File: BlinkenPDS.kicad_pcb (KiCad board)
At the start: 4 copper layers, 129 x 99 mm, 257 parts, among them CN1 PDS_LB_MALE, CN2 PDS_PT_FEMALE RA, CN3 PDS_PT_FEMALE ST, U1 74HC14D, U10 74HC14D, U11 74HC14D, U12 74HC14D, U13 74HC14D, U14 74HC14D, U15 74HC14D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

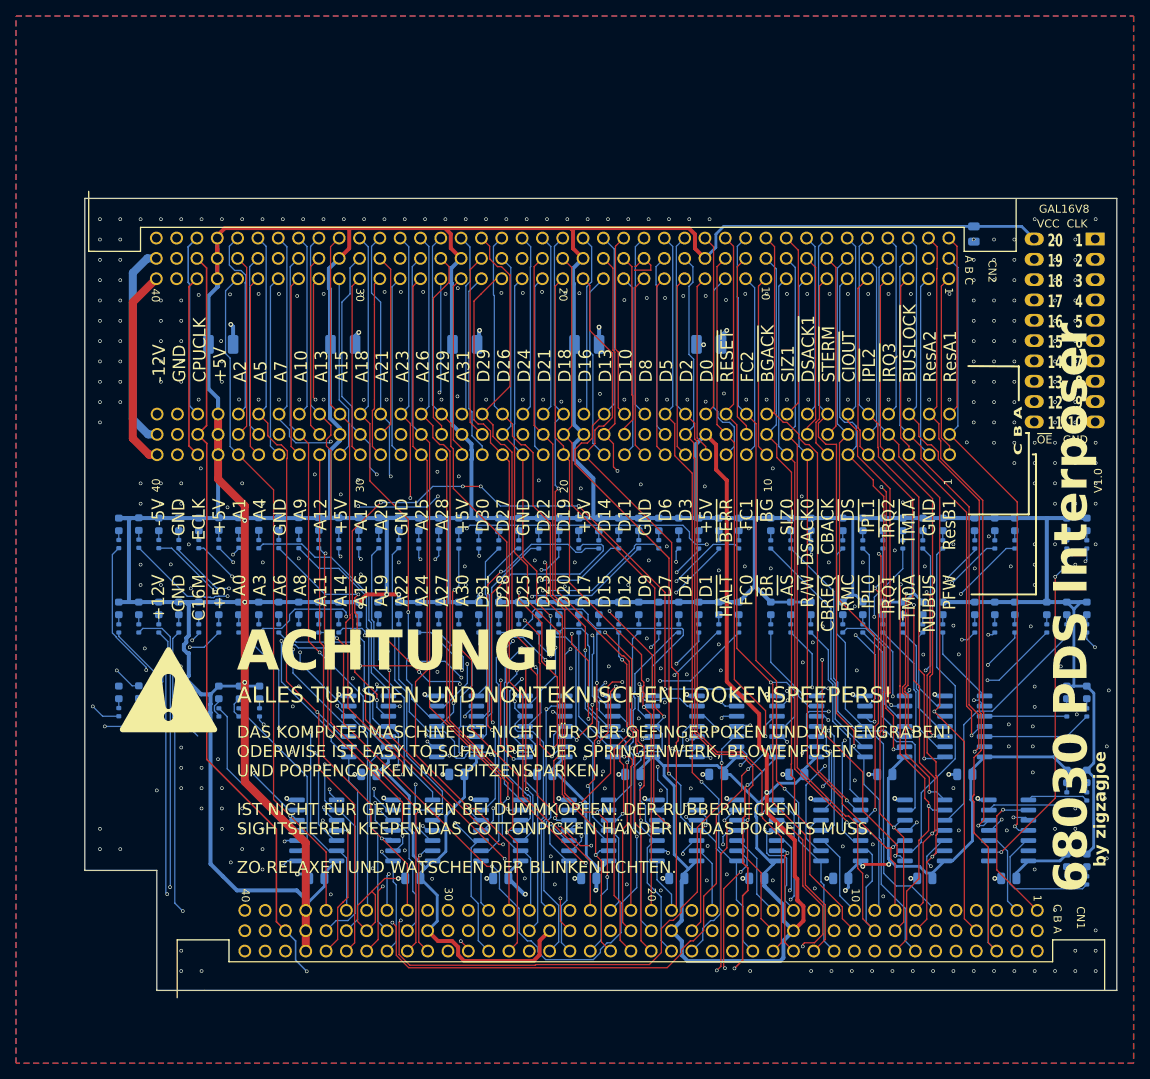
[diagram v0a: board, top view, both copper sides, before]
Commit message: remove PFW, add CACHE, updated production files
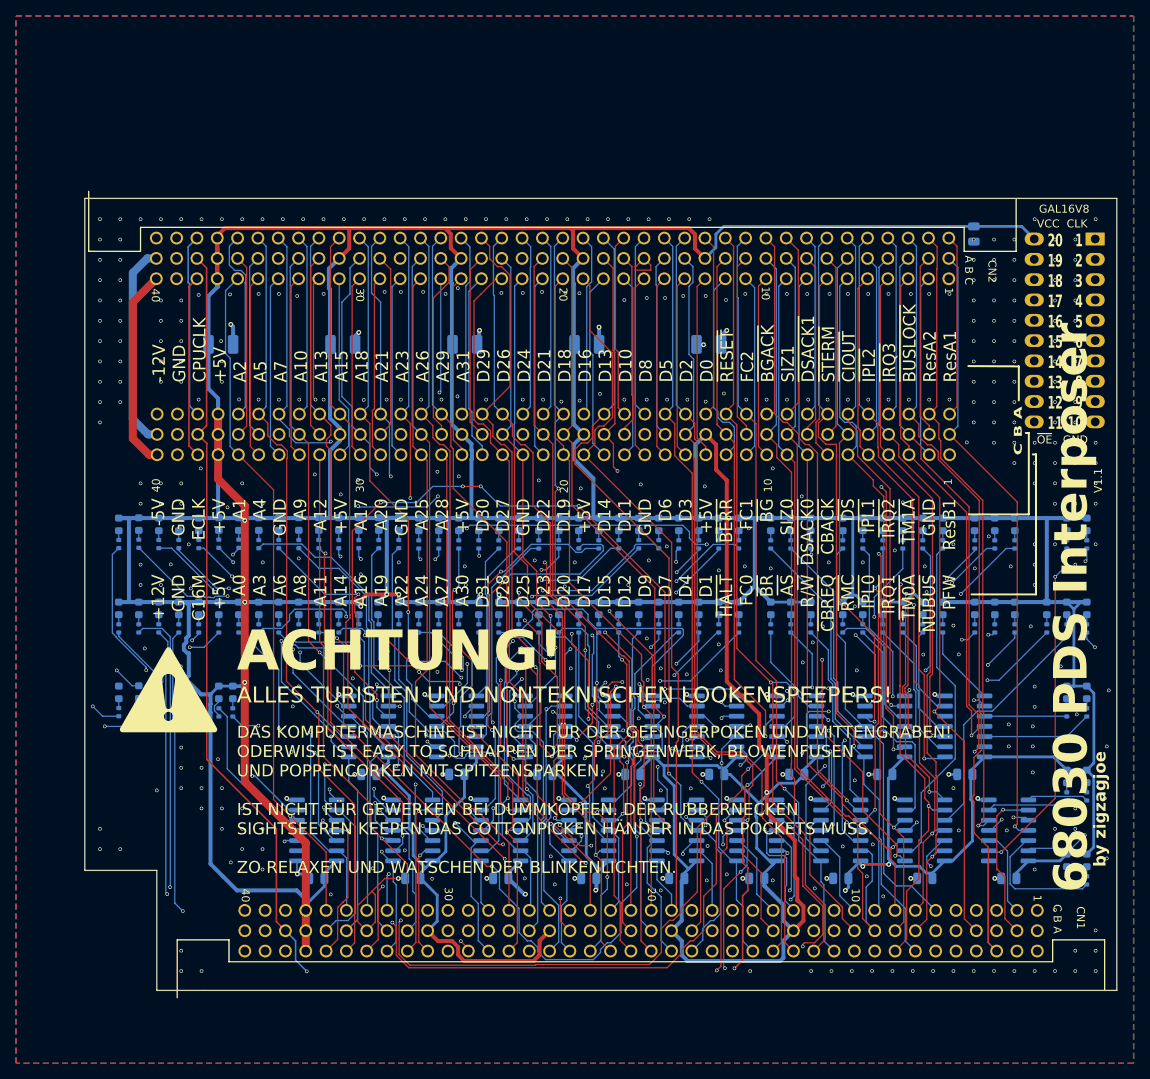
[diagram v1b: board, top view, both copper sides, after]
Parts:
- removed D67: C, SockeBooster:LED_0603_1608Metric_Label
- removed R68: 510, SockeBooster:R_0402_1005Metric_NoLabel
- moved D66 3.34 mm to (90.5, 93.8)
- moved R67 3.34 mm to (90.5, 96.2)
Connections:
- CN1 pad B2: GND -> /CACHE
- CN1 pad C1: /PFW -> unconnected-(CN1-PFW-PadC1)
- CN2 pad B2: GND -> /CACHE
- CN2 pad C1: /PFW -> unconnected-(CN2-PFW-PadC1)
- CN3 pad B2: GND -> /CACHE
- CN3 pad C1: /PFW -> unconnected-(CN3-PFW-PadC1)
- U1 pad 1: /C16M -> GND
- U1 pad 2: Net-(U1-O1) -> unconnected-(U1-O1-Pad2)
- U13 pad 13: unconnected-(U13-I6-Pad13) -> /RESA1
- U13 pad 9: /PFW -> /CACHE
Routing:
- net /CACHE: track 0.00 -> 94.3 mm, vias 0 -> 1
- net /PFW: track 88.2 -> 0.00 mm, vias 1 -> 0
- net Net-(U1-O1): track 21.7 -> 0.00 mm
- net /RESA1: track 100.0 -> 107.7 mm, vias 0 -> 1
- net Net-(D67-K): track 2.74 -> 0.00 mm
- net Net-(U6-O1): track 105.0 -> 107.6 mm
- net /C16M: track 86.6 -> 84.6 mm, vias 1 -> 0
- net GND: track 120.9 -> 119.2 mm
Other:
- board text added: "V1.1"
- board text removed: "V1.0"
